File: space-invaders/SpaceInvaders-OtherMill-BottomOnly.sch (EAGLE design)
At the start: 26 parts, among them J2_J4 TM4C123GXL, J3_J1 TM4C123GXL, J5 Nokia 5110, J6 Nokia 5110, U1 5V Voltage Regulator

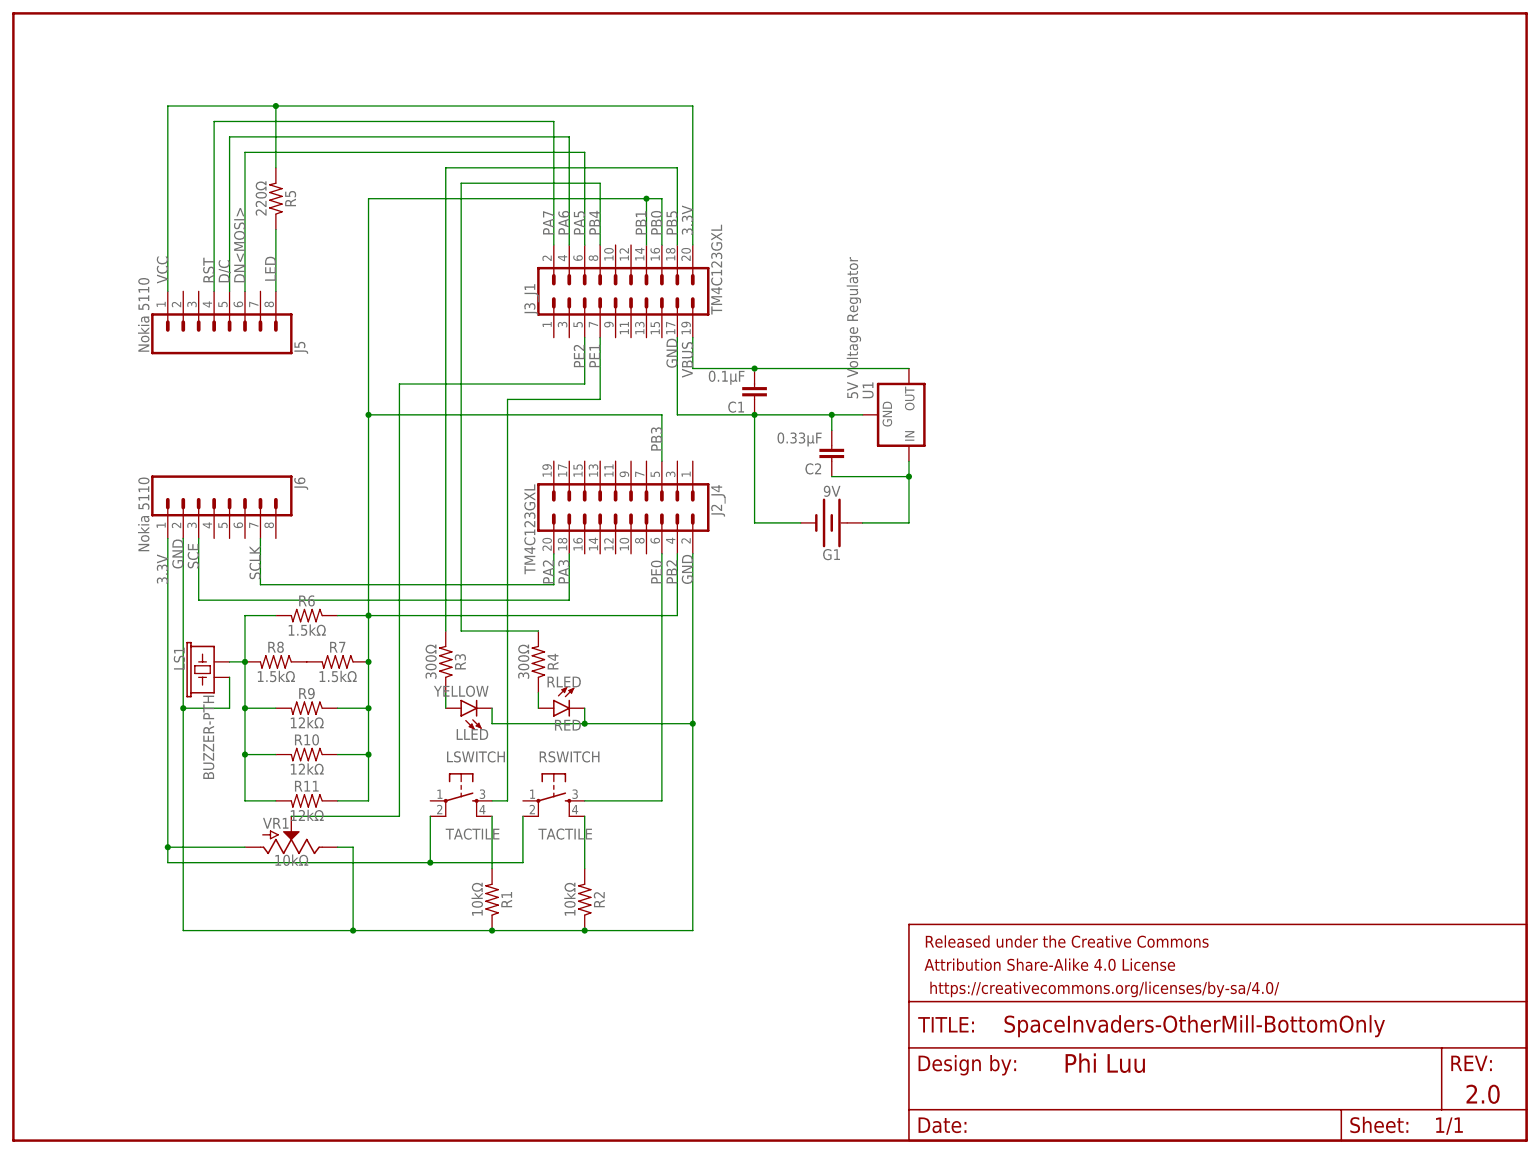
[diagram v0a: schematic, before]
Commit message: Reposition SpaceInvaders board layout
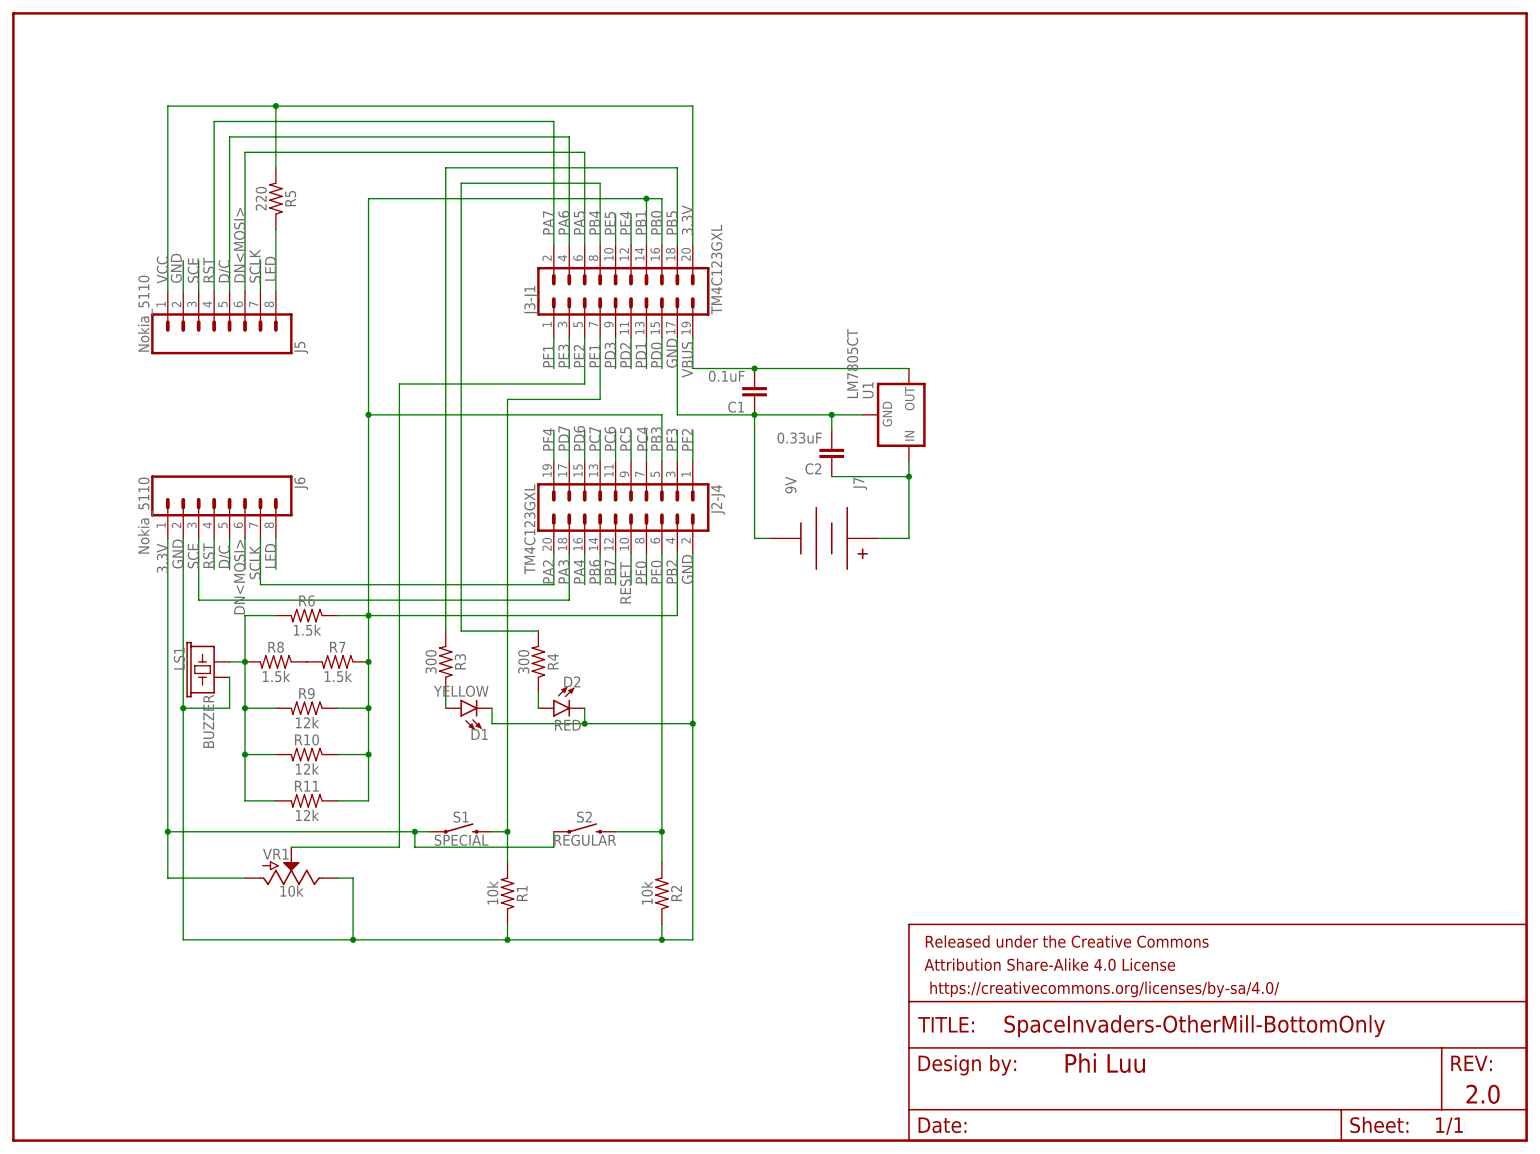
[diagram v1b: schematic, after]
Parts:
- removed G1: 9V, SparkFun-Batteries:BATTERY-9V
- removed LSWITCH, RSWITCH: TACTILE, SparkFun-Retired:TAC_SWITCHPTH
- added J7: 9V, SparkFun-Connectors:BC9VPC
- added S1: SPECIAL, SparkFun-Switches:MOMENTARY-SWITCH-SPST-PTH-6.0MM
- added S2: REGULAR, SparkFun-Switches:MOMENTARY-SWITCH-SPST-PTH-6.0MM
- C1: value 0.1μF -> 0.1uF
- C2: value 0.33μF -> 0.33uF
- J5, J6: value Nokia 5110 -> Nokia_5110
- LS1: value BUZZER-PTH -> BUZZER
- R1, R2, VR1: value 10kΩ -> 10k
- R10, R11, R9: value 12kΩ -> 12k
- R3, R4: value 300Ω -> 300
- R5: value 220Ω -> 220
- R6, R7, R8: value 1.5kΩ -> 1.5k
- U1: value 5V Voltage Regulator -> LM7805CT
- renumbered J2_J4 to J2-J4, J3_J1 to J3-J1, LLED to D1, RLED to D2
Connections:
- net N$17 renamed RLED
- net N$19 renamed LLED
- net N$23 renamed DAC_OUT
- removed net N$12: LSWITCH.4, R1.2
- removed net N$14: R2.2, RSWITCH.4
- new net D/C: J6.5
- new net DN<MOSI>: J6.6
- new net PA4: J2-J4.16
- new net PB6: J2-J4.14
- new net PB7: J2-J4.12
- new net PC4: J2-J4.7
- new net PC5: J2-J4.9
- new net PC6: J2-J4.11
- new net PC7: J2-J4.13
- new net PD0: J3-J1.15
- new net PD1: J3-J1.13
- new net PD2: J3-J1.11
- new net PD3: J3-J1.9
- new net PD6: J2-J4.15
- new net PD7: J2-J4.17
- new net PE3: J3-J1.3
- new net PE4: J3-J1.12
- new net PE5: J3-J1.10
- new net PF0: J2-J4.8
- new net PF1: J3-J1.1
- new net PF2: J2-J4.1
- new net PF3: J2-J4.3
- new net PF4: J2-J4.19
- new net RESET: J2-J4.10
- new net RST: J6.4
- new net SCE: J5.3
- new net SCLK: J5.7
- net 3.3V: now also S1.1, S2.1; no longer LSWITCH.2, RSWITCH.2
- net 9V: now also J7.V+; no longer G1.+
- net GND: now also J5.2, J7.V-; no longer G1.-
- net LED: now also J6.8
- net PE0: now also R2.2, S2.2; no longer RSWITCH.3
- net PE1: now also R1.2, S1.2; no longer LSWITCH.3
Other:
- moved on the sheet: R1, R2, VR1

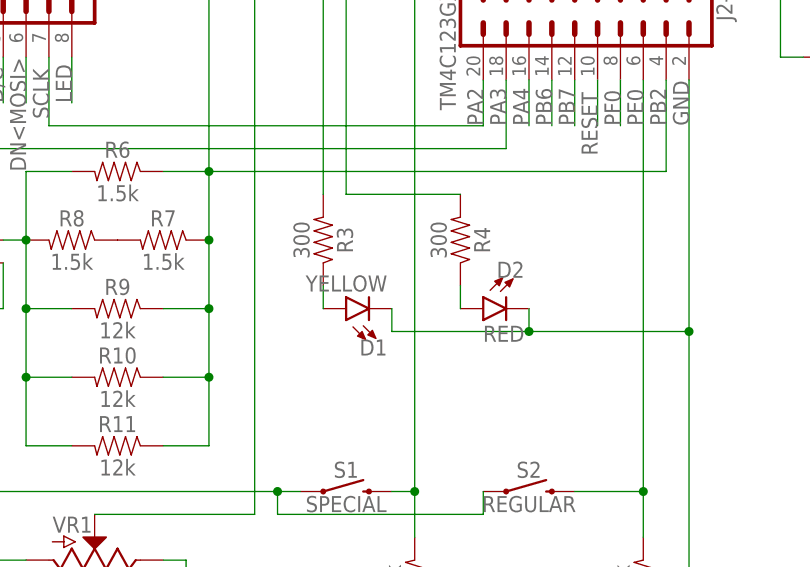
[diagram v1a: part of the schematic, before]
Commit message: Change LLED and RLED resistor value from 300 to 220
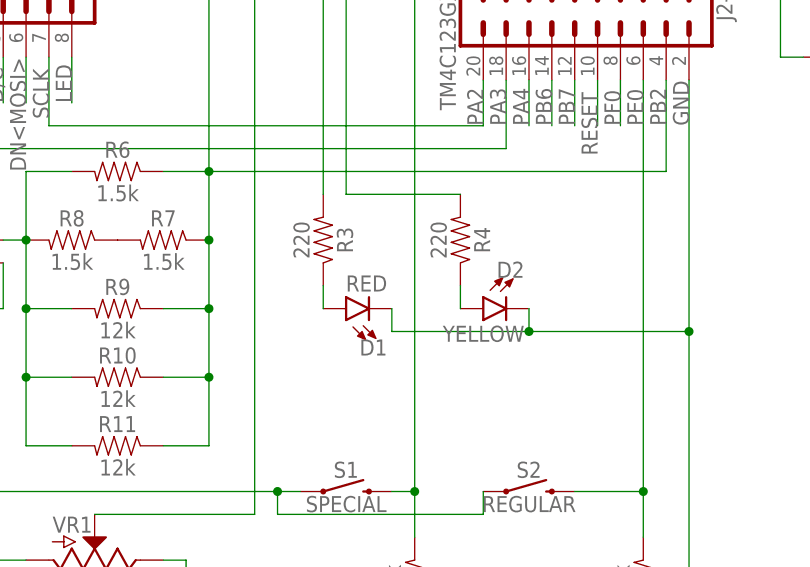
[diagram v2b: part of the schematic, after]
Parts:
- D1: value YELLOW -> RED
- D2: value RED -> YELLOW
- R3, R4: value 300 -> 220
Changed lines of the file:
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@@
 <part name="LS1" library="SparkFun-Electromechanical" deviceset="BUZZER" device="-PTH" value="BUZZER"/>
 <part name="VR1" library="SparkFun-Resistors" deviceset="POTENTIOMETER_SLIDE" device="-30MM-1/10W-20%" value="10k"/>
-<part name="D1" library="SparkFun-LED" deviceset="LED" device="5MM" value="YELLOW"/>
-<part name="D2" library="SparkFun-LED" deviceset="LED" device="5MM" value="RED"/>
+<part name="D1" library="SparkFun-LED" deviceset="LED" device="5MM" value="RED"/>
+<part name="D2" library="SparkFun-LED" deviceset="LED" device="5MM" value="YELLOW"/>
 <part name="R1" library="SparkFun-Resistors" deviceset="10KOHM" device="-HORIZ-1/4W-5%" value="10k"/>
 <part name="R2" library="SparkFun-Resistors" deviceset="10KOHM" device="-HORIZ-1/4W-5%" value="10k"/>
-<part name="R3" library="SparkFun-Resistors" deviceset="1KOHM" device="-HORIZ-1/4W-5%" value="300"/>
-<part name="R4" library="SparkFun-Resistors" deviceset="1KOHM" device="-HORIZ-1/4W-5%" value="300"/>
+<part name="R3" library="SparkFun-Resistors" deviceset="1KOHM" device="-HORIZ-1/4W-5%" value="220"/>
+<part name="R4" library="SparkFun-Resistors" deviceset="1KOHM" device="-HORIZ-1/4W-5%" value="220"/>
 <part name="R5" library="SparkFun-Resistors" deviceset="1KOHM" device="-HORIZ-1/4W-5%" value="220"/>
 <part name="R6" library="SparkFun-Resistors" deviceset="1KOHM" device="-HORIZ-1/4W-5%" value="1.5k"/>
